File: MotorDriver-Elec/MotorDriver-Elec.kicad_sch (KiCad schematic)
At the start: 22 parts, among them J4 B2B-XH-ALFSN, U1 Pico, U2 ULN2003A

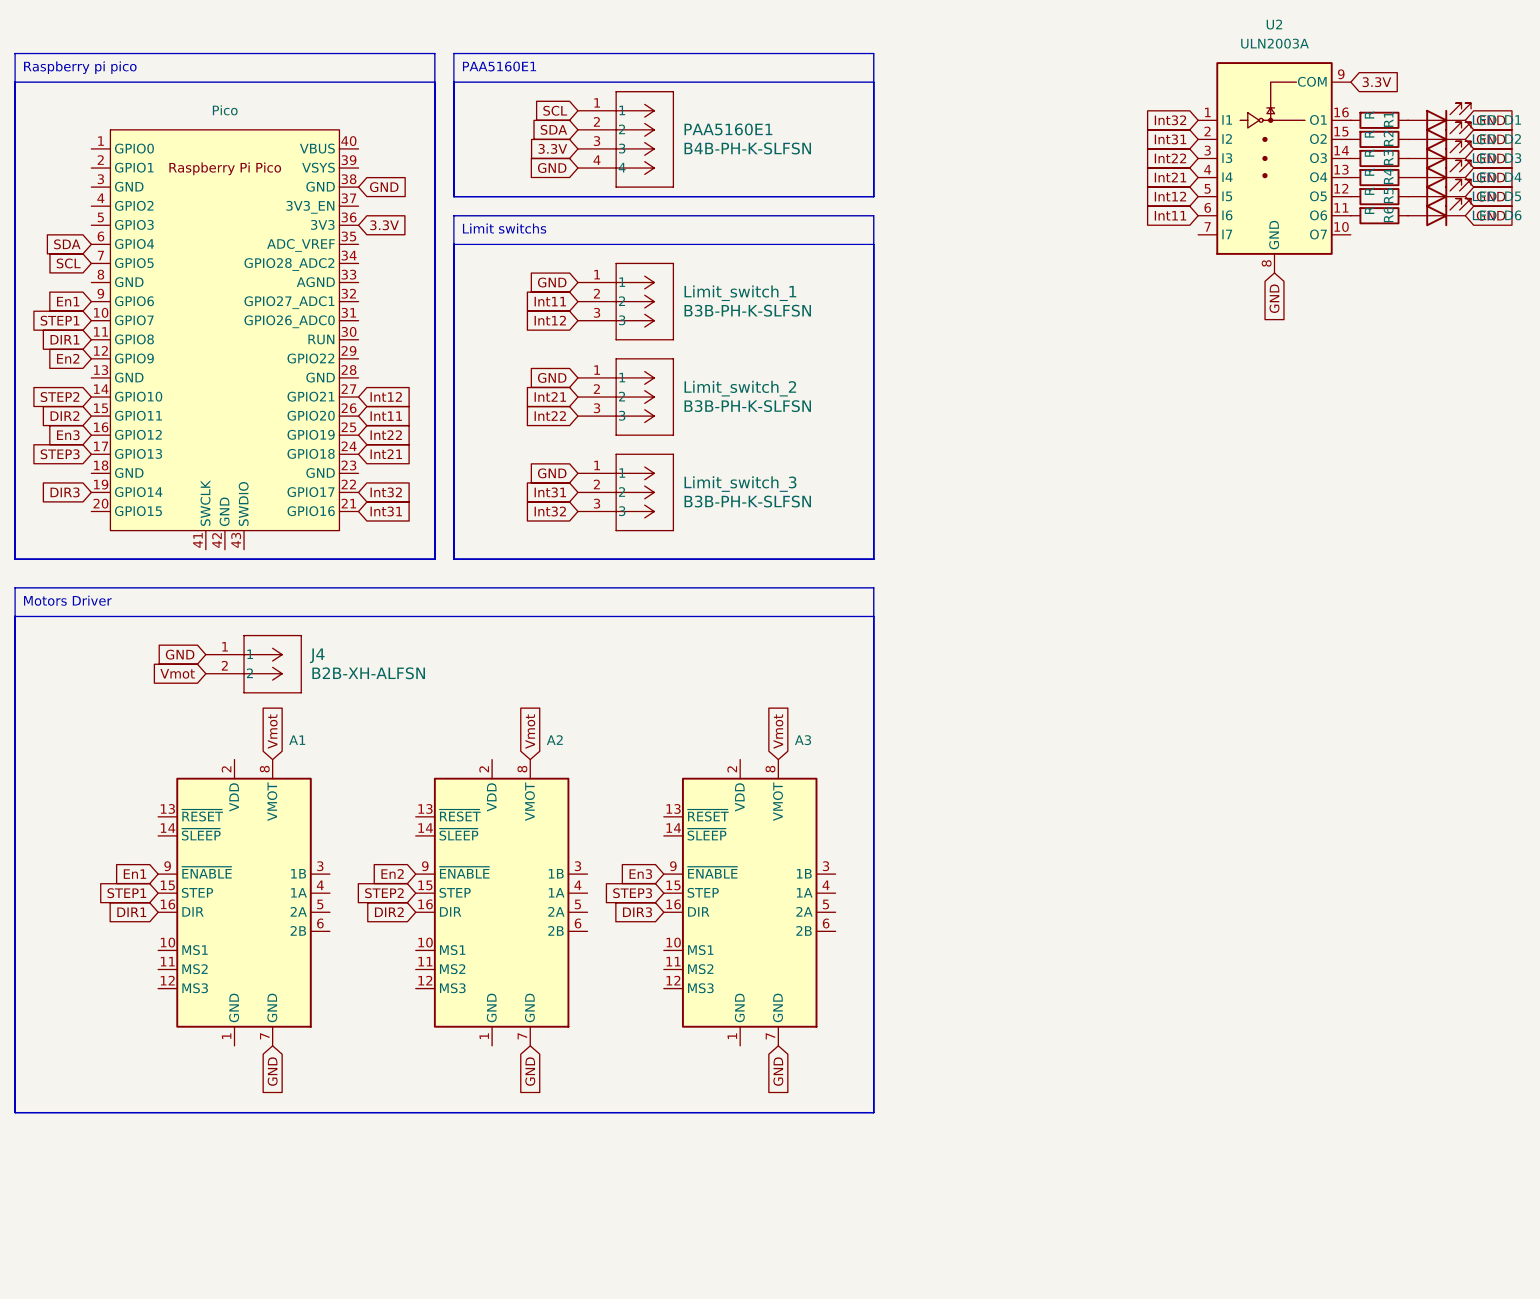
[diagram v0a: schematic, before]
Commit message: Feat: add LED indicators
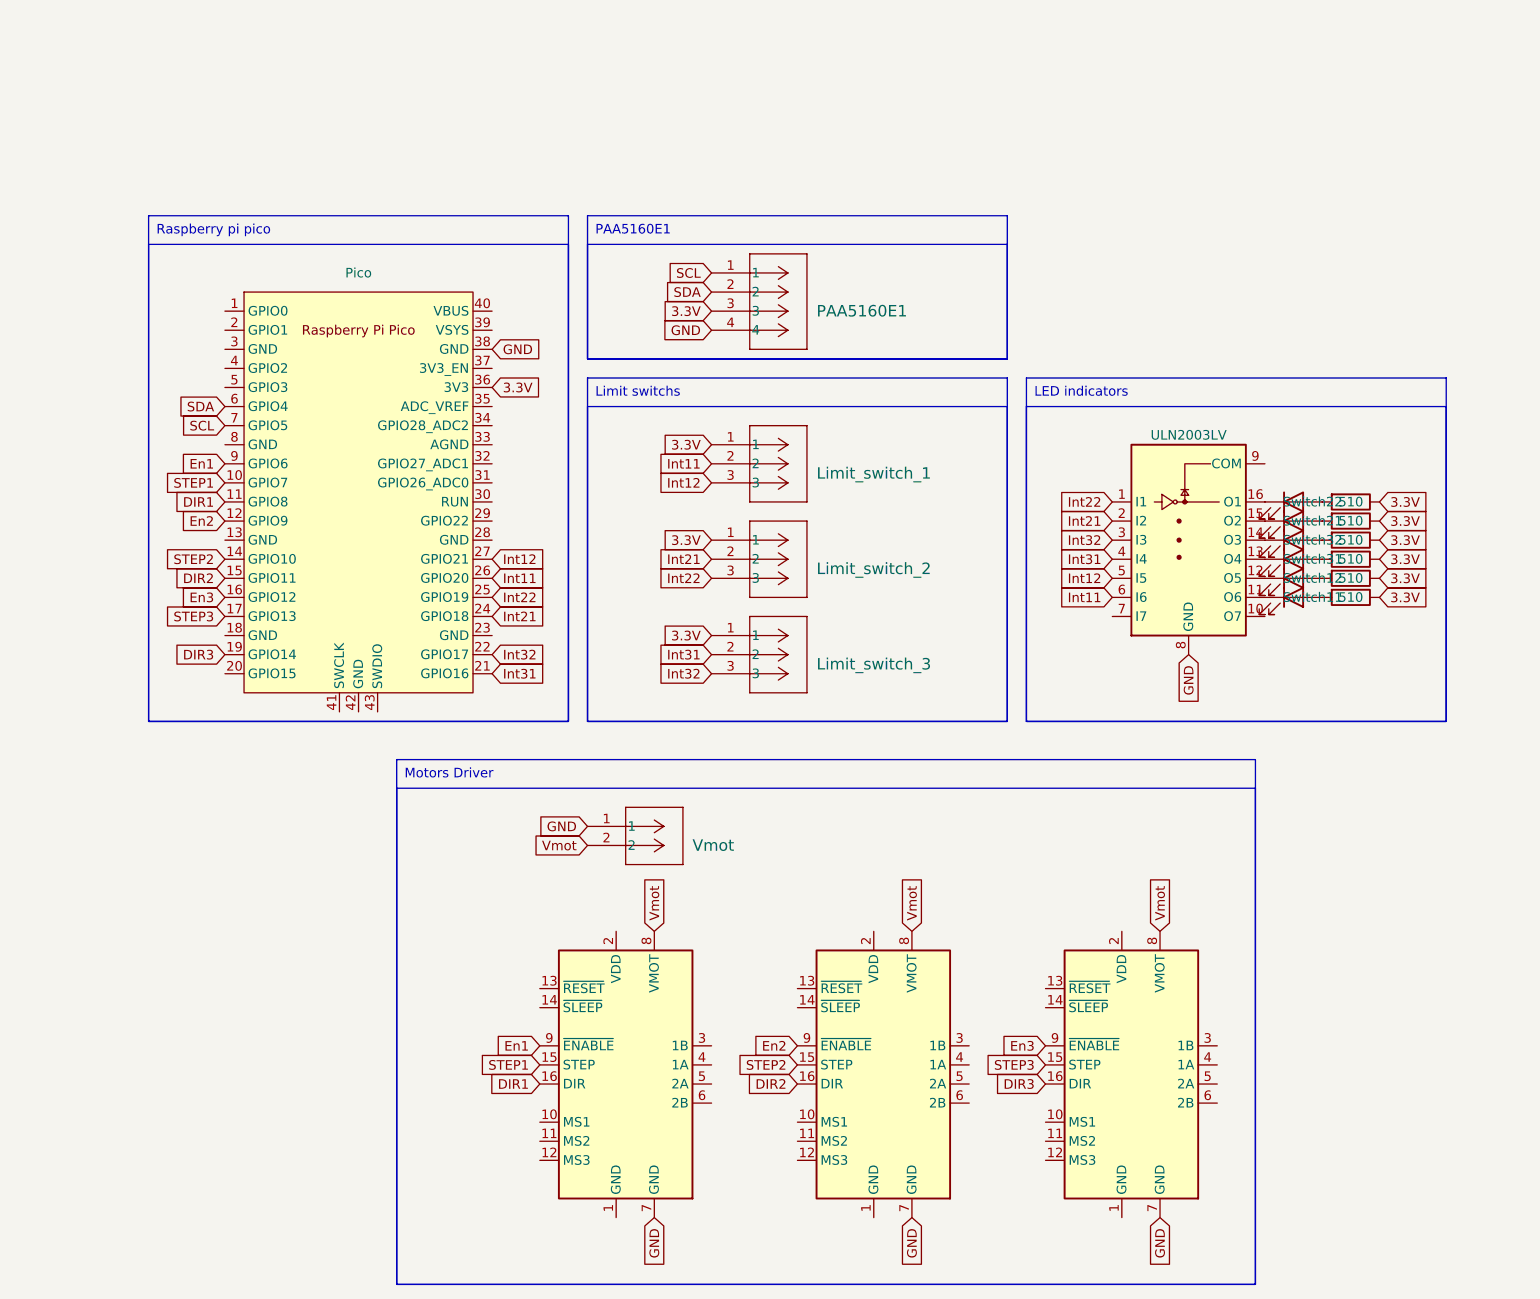
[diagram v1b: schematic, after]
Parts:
- removed D1, D2, D3, D4, D5, D6: LED, LED_THT:LED_D3.0mm, symbol Device:LED
- removed U2: ULN2003A, Package_DIP:DIP-16_W7.62mm_Socket, symbol Transistor_Array:ULN2003A
- added Switch11: Switch11, LED_THT:LED_D3.0mm_Horizontal_O1.27mm_Z2.0mm, symbol Device:LED
- added Switch12: Switch12, LED_THT:LED_D3.0mm_Horizontal_O1.27mm_Z2.0mm, symbol Device:LED
- added Switch21: Switch21, LED_THT:LED_D3.0mm_Horizontal_O1.27mm_Z2.0mm, symbol Device:LED
- added Switch22: Switch22, LED_THT:LED_D3.0mm_Horizontal_O1.27mm_Z2.0mm, symbol Device:LED
- added Switch31: Switch31, LED_THT:LED_D3.0mm_Horizontal_O1.27mm_Z2.0mm, symbol Device:LED
- added Switch32: Switch32, LED_THT:LED_D3.0mm_Horizontal_O1.27mm_Z2.0mm, symbol Device:LED
- added U3: ULN2003LV, Package_SO:SOIC-16_3.9x9.9mm_P1.27mm, symbol Transistor_Array:ULN2003A
- A1: value Pololu_Breakout_A4988 -> MKS_MotorDriver_1
- A2: value Pololu_Breakout_A4988 -> MKS_MotorDriver_2
- A3: value Pololu_Breakout_A4988 -> MKS_MotorDriver_3
- J4: value B2B-XH-ALFSN -> Vmot
- Limit_switch_1: value B3B-PH-K-SLFSN -> Limit_switch_1
- Limit_switch_2: value B3B-PH-K-SLFSN -> Limit_switch_2
- Limit_switch_3: value B3B-PH-K-SLFSN -> Limit_switch_3
- PAA5160E1: value B4B-PH-K-SLFSN -> PAA5160E1
- R1, R2, R3, R4, R5, R6: value R -> 510
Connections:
- net 3.3V: now also Limit_switch_1.1, Limit_switch_2.1, Limit_switch_3.1, R1.1, R2.1, R3.1, R4.1, R5.1, R6.1
- net GND: now also U3.8 (GND); no longer Limit_switch_1.1, Limit_switch_2.1, Limit_switch_3.1
- net Int11: now also U3.6 (I6)
- net Int12: now also U3.5 (I5)
- net Int21: now also U3.2 (I2)
- net Int22: now also U3.1 (I1)
- net Int31: now also U3.4 (I4)
- net Int32: now also U3.3 (I3)
- net at R3.2: now also Switch32.2 (A)
- net at R1.2: now also Switch22.2 (A)
- net at R6.2: now also Switch11.2 (A)
- net at R5.2: now also Switch12.2 (A)
- net at R4.2: now also Switch31.2 (A)
- net at R2.2: now also Switch21.2 (A)
- new net: Switch12.1 (K), U3.12 (O5)
- new net: Switch22.1 (K), U3.16 (O1)
- new net: Switch31.1 (K), U3.13 (O4)
- new net: Switch11.1 (K), U3.11 (O6)
- new net: Switch32.1 (K), U3.14 (O3)
- new net: Switch21.1 (K), U3.15 (O2)

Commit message: Fix: space between LEDs
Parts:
- removed U3: ULN2003LV, Package_SO:SOIC-16_3.9x9.9mm_P1.27mm, symbol Transistor_Array:ULN2003A
- added UN2003LV1: UN2003LV, Package_SO:SOIC-16_3.9x9.9mm_P1.27mm, symbol Transistor_Array:ULN2003A
- renumbered J4 to Vmot1
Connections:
- net GND: now also UN2003LV1.8 (GND)
- net Int11: now also UN2003LV1.6 (I6)
- net Int12: now also UN2003LV1.5 (I5)
- net Int21: now also UN2003LV1.2 (I2)
- net Int22: now also UN2003LV1.1 (I1)
- net Int31: now also UN2003LV1.4 (I4)
- net Int32: now also UN2003LV1.3 (I3)
- net at Switch12.1 (K): now also UN2003LV1.12 (O5)
- net at Switch22.1 (K): now also UN2003LV1.16 (O1)
- net at Switch31.1 (K): now also UN2003LV1.13 (O4)
- net at Switch11.1 (K): now also UN2003LV1.11 (O6)
- net at Switch32.1 (K): now also UN2003LV1.14 (O3)
- net at Switch21.1 (K): now also UN2003LV1.15 (O2)
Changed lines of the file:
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@@
   )
   (symbol (lib_id "Transistor_Array:ULN2003A") (at 172.72 82.55 0) (unit 1)
-    (in_bom yes) (on_board yes) (dnp no)
-    (property "Reference" "U3" (at 172.72 64.77 0)
-      (effects (font (size 1.27 1.27)) hide)
-    )
-    (property "Value" "ULN2003LV" (at 172.72 68.58 0)
+    (in_bom yes) (on_board yes) (dnp no) (fields_autoplaced)
+    (property "Reference" "UN2003LV1" (at 172.72 64.77 0)
+      (effects (font (size 1.27 1.27)) hide)
+    )
+    (property "Value" "UN2003LV" (at 172.72 67.31 0)
       (effects (font (size 1.27 1.27)))
     )
@@
       (effects (font (size 1.27 1.27)) hide)
     )
+    (pin "5")
     (pin "4")
+    (pin "3")
+    (pin "6")
+    (pin "12")
+    (pin "7")
+    (pin "2")
+    (pin "10")
+    (pin "11")
     (pin "8")
-    (pin "2")
-    (pin "11")
-    (pin "1")
-    (pin "16")
-    (pin "10")
-    (pin "12")
+    (pin "9")
     (pin "13")
-    (pin "6")
-    (pin "7")
-    (pin "5")
-    (pin "9")
-    (pin "3")
     (pin "14")
     (pin "15")
-    (instances
-      (project "MotorDriver-Elec"
-        (path "/900535aa-6f11-4883-8834-dba1c48b902e"
-          (reference "U3") (unit 1)
+    (pin "1")
+    (pin "16")
+    (instances
+      (project "MotorDriver-Elec"
+        (path "/900535aa-6f11-4883-8834-dba1c48b902e"
+          (reference "UN2003LV1") (unit 1)
         )
       )
@@
   (symbol (lib_id "CONN_B2B-XH-ALFSN_JST:B2B-XH-ALFSN") (at 92.71 120.65 0) (unit 1)
     (in_bom yes) (on_board yes) (dnp no) (fields_autoplaced)
-    (property "Reference" "J4" (at 106.68 120.65 0)
+    (property "Reference" "Vmot1" (at 106.68 120.65 0)
       (effects (font (size 1.524 1.524)) (justify left) hide)
     )
@@
       (project "MotorDriver-Elec"
         (path "/900535aa-6f11-4883-8834-dba1c48b902e"
-          (reference "J4") (unit 1)
-        )
-      )
+          (reference "Vmot1") (unit 1)
+        )
+      )
